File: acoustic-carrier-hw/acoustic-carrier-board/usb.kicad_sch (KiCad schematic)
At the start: 30 parts, among them J4 TYPE-C-31-M-12, U15 USB3300-EZK, U6 TS3USB30EDGSR, Y3 Crystal_GND24_Small

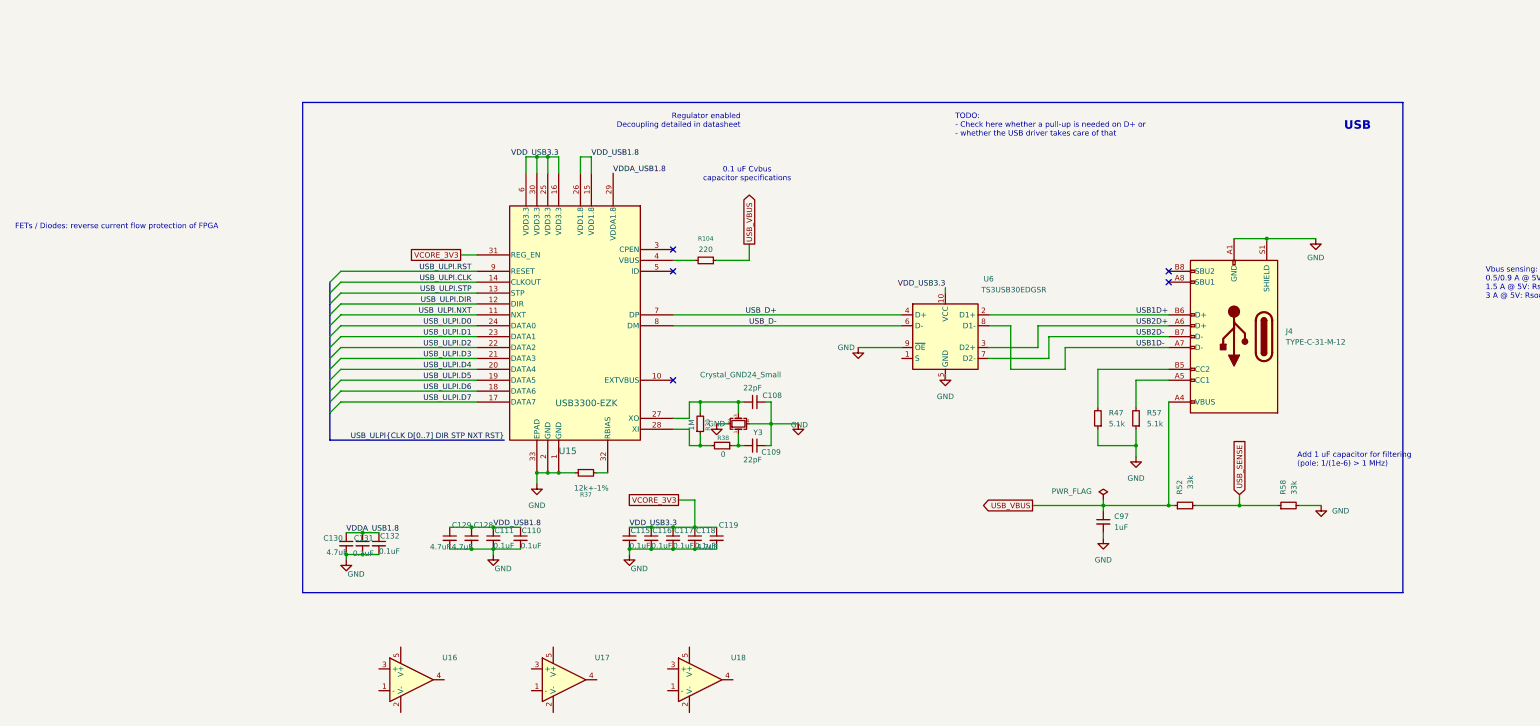
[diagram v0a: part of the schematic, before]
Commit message: [carrier] Finished schmitt trigger for cc1 and cc2 led driver + passive power signalling
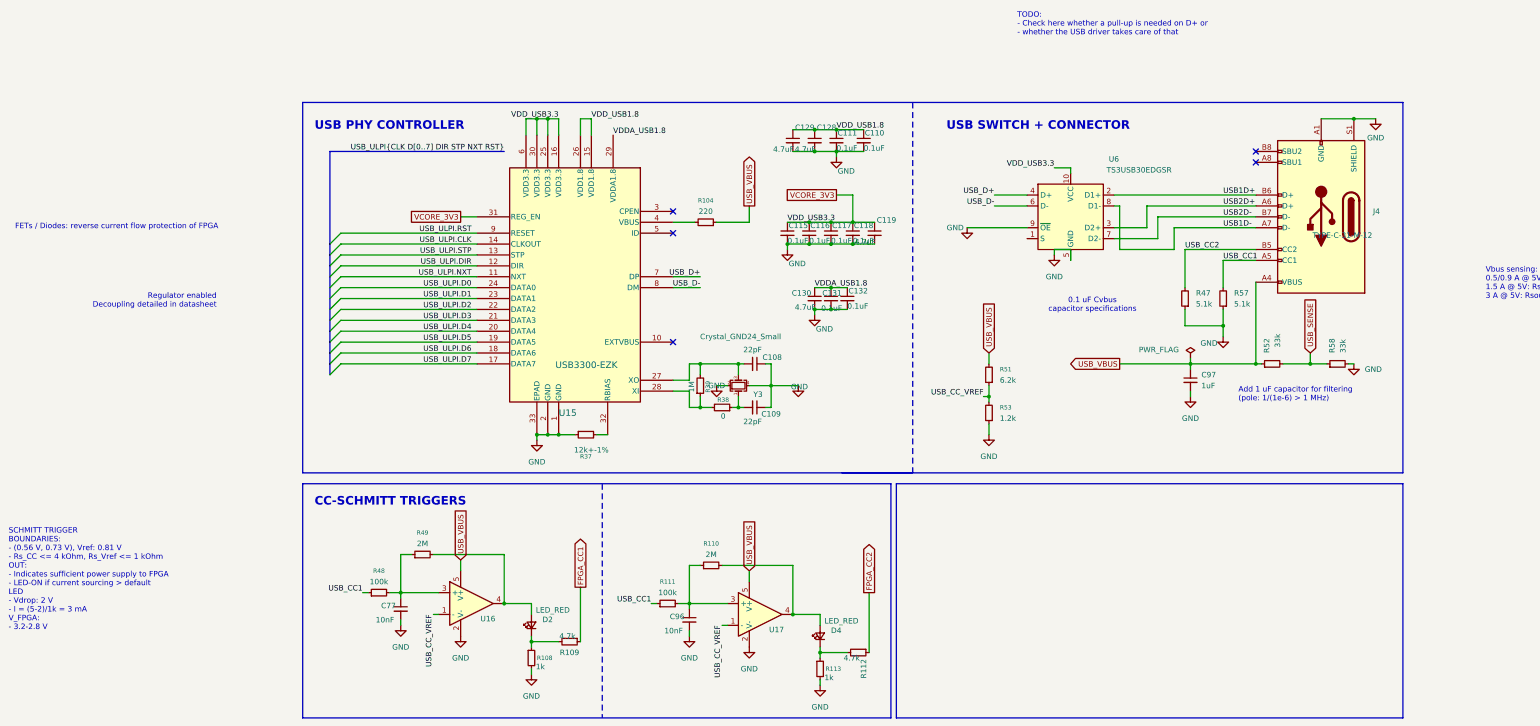
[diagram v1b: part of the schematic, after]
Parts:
- removed U18: ~, Package_TO_SOT_SMD:SOT-23-5, symbol COS3201:COS3201
- added C77, C96: 10nF, symbol Device:C_Small
- added D2, D4: LED_RED, Resistor_SMD:R_0603_1608Metric, symbol Device:LED_Small
- added R108, R113: 1k, Resistor_SMD:R_0603_1608Metric, symbol Device:R_Small
- added R109, R112: 4.7k, Resistor_SMD:R_0402_1005Metric, symbol Device:R_Small
- added R110, R49: 2M, Resistor_SMD:R_0603_1608Metric_Pad0.98x0.95mm_HandSolder, symbol Device:R_Small
- added R111, R48: 100k, Resistor_SMD:R_0603_1608Metric_Pad0.98x0.95mm_HandSolder, symbol Device:R_Small
- added R51: 6.2k, Resistor_SMD:R_0603_1608Metric_Pad0.98x0.95mm_HandSolder, symbol Device:R_Small
- added R53: 1.2k, Resistor_SMD:R_0603_1608Metric_Pad0.98x0.95mm_HandSolder, symbol Device:R_Small
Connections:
- net GND: now also U16.2 (V-), U17.2 (V-), C77.2, C96.2, R108.2, R113.2, R53.1
- net USB_VBUS: now also U16.5 (V+), U17.5 (V+), R51.2
- net USB_CC1: now reaches J4.A5 (CC1), R57.2
- net USB_CC1: now also R111.1, R48.1
- net USB_CC2: now reaches J4.B5 (CC2), R47.2
- net USB_CC_VREF: now reaches U17.1 (-)
- net USB_CC_VREF: now also U16.1 (-), R51.1, R53.2
- net at U17.3 (+): now also C96.1, R110.1, R111.2
- net at U17.4: now also D4.2 (A), R110.2
- net at U16.3 (+): now also C77.1, R48.2, R49.1
- net at U16.4: now also D2.2 (A), R49.2
- new net: D2.1 (K), R108.1, R109.2
- new net: D4.1 (K), R112.2, R113.1
- new net FPGA_CC1: R109.1
- new net FPGA_CC2: R112.1
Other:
- note added: "SCHMITT TRIGGER BOUNDARIES: - (0.56 V, 0.73 V), Vref: 0.81 V - Rs_CC <= 4 kOhm, Rs_Vref <= 1 kOhm OUT: - Indicates sufficient power supply to FPGA - LED-ON if current sourcing > default LED - Vdrop: 2 V - I = (5-2)/1k = 3 mA V_FPGA: - 3.2-2.8 V"
- moved on the sheet: C108, C109, C110, C111, C115, C116, C117, C118, C119, C128, C129, C130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

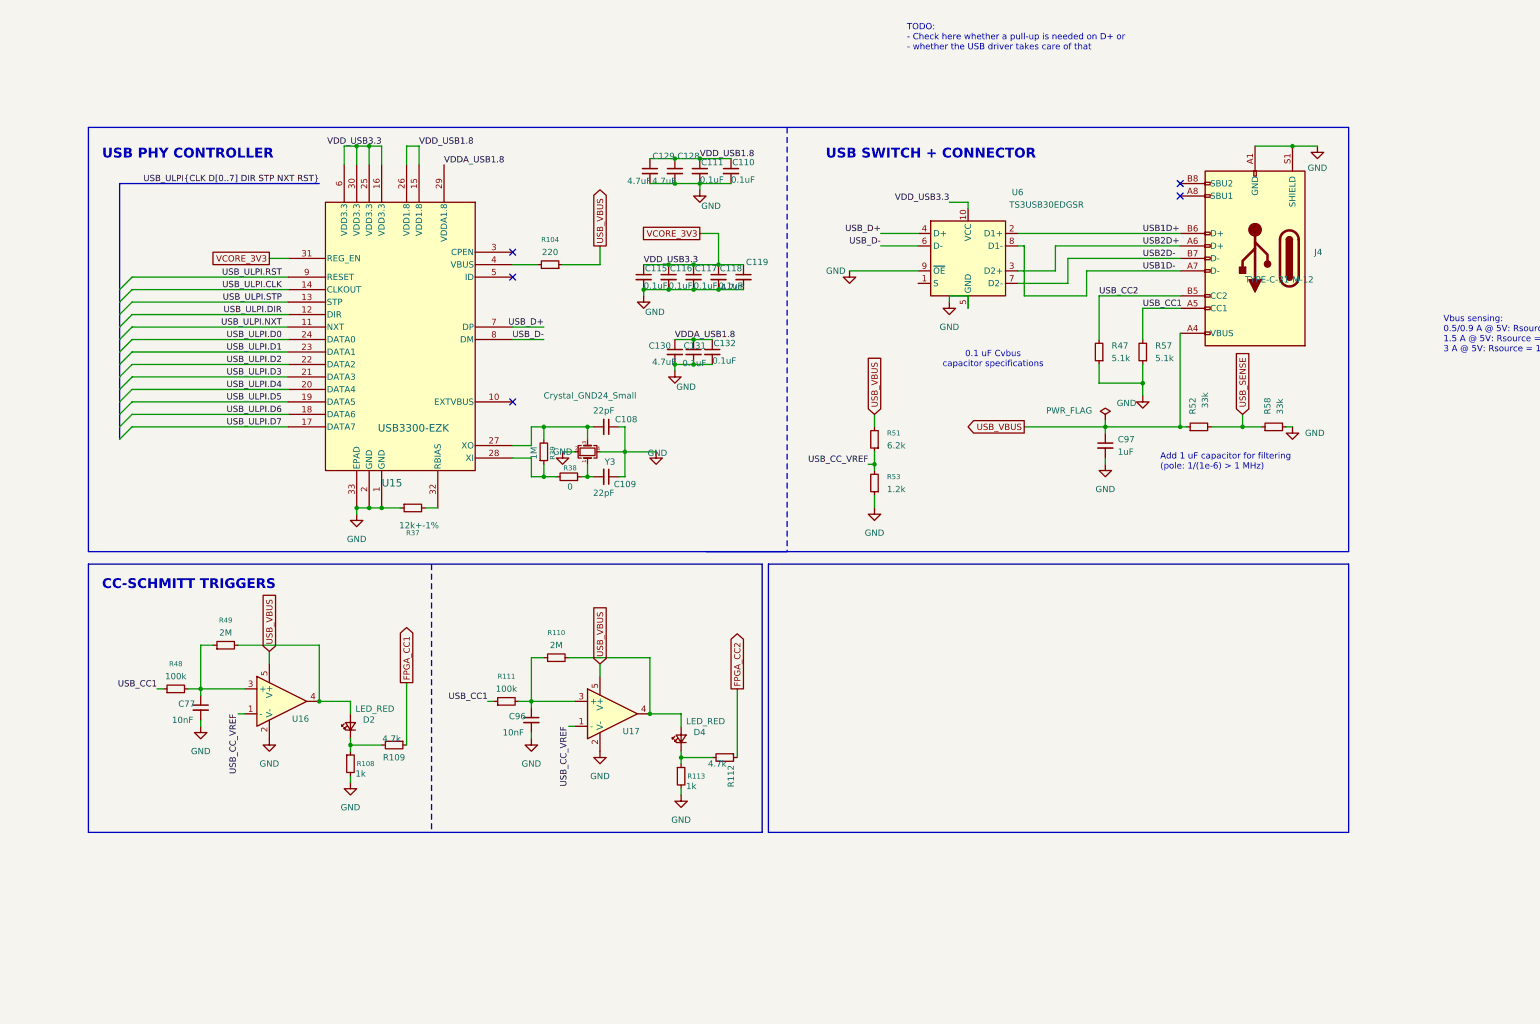
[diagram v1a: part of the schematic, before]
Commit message: [carrier] Added schmitt trigger for switch (next) check if well-connected (polarity)
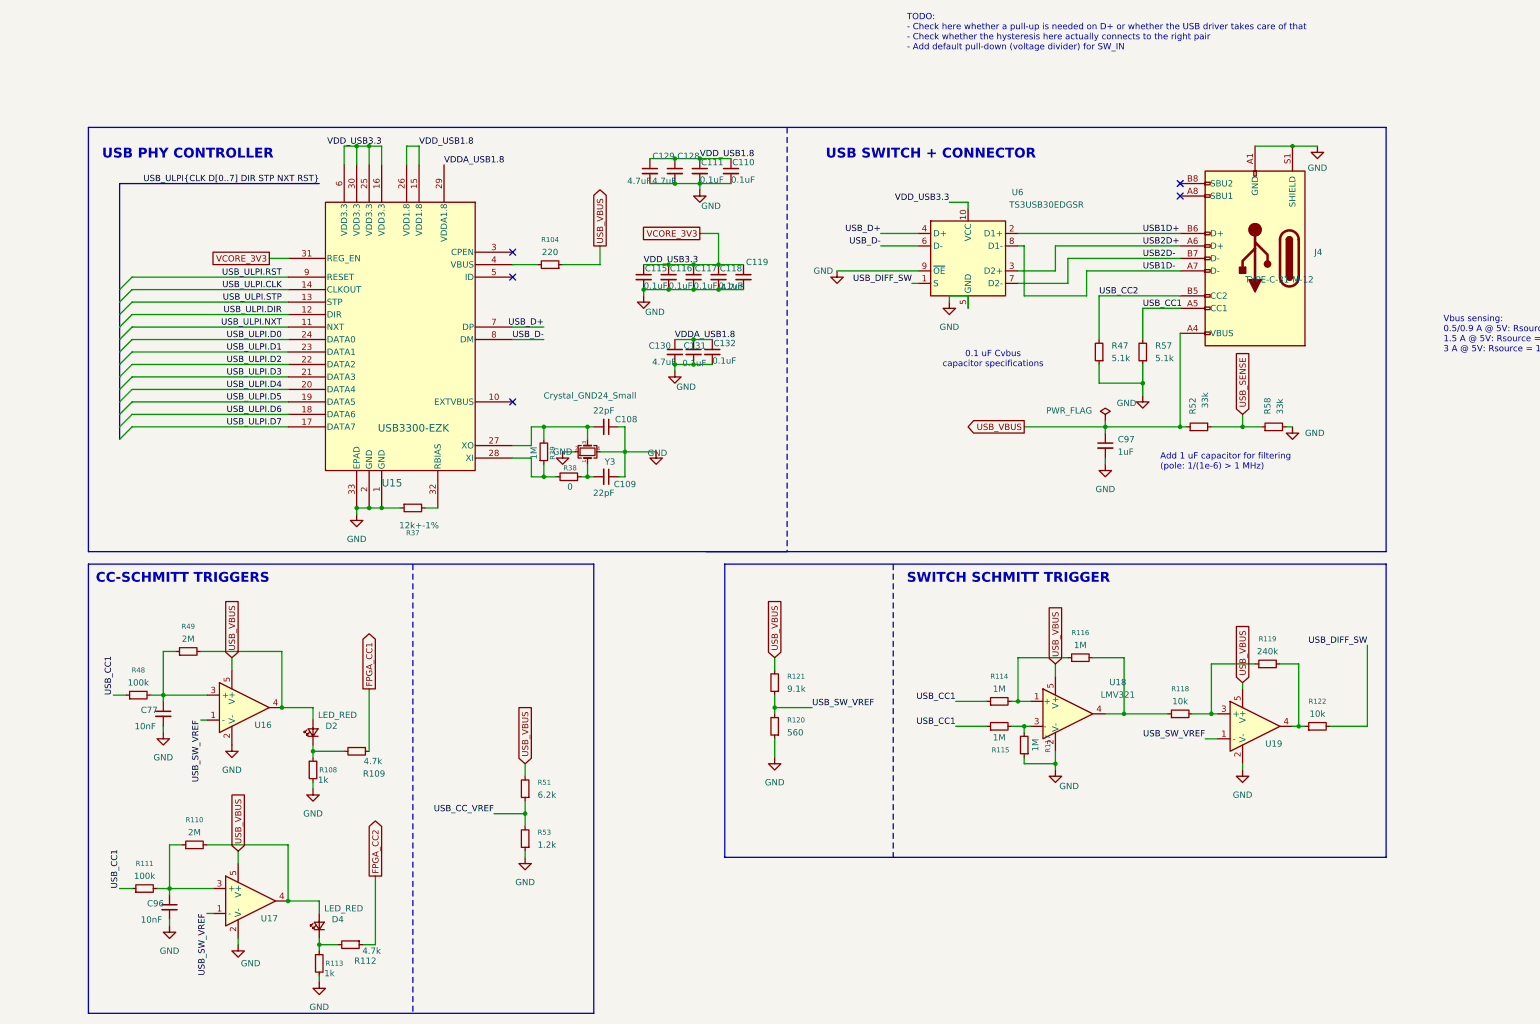
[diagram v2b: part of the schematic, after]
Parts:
- added R114, R115, R116, R117: 1M, Resistor_SMD:R_0603_1608Metric_Pad0.98x0.95mm_HandSolder, symbol Device:R_Small
- added R118, R122: 10k, Resistor_SMD:R_0603_1608Metric, symbol Device:R_Small
- added R119: 240k, Resistor_SMD:R_0603_1608Metric, symbol Device:R_Small
- added R120: 560, Resistor_SMD:R_0603_1608Metric_Pad0.98x0.95mm_HandSolder, symbol Device:R_Small
- added R121: 9.1k, Resistor_SMD:R_0603_1608Metric_Pad0.98x0.95mm_HandSolder, symbol Device:R_Small
- added U18: LMV321, Package_TO_SOT_SMD:SOT-23-5, symbol Amplifier_Operational:LMV321
- added U19: ~, Package_TO_SOT_SMD:SOT-23-5, symbol COS3201:COS3201
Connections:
- net GND: now also R117.1, R120.1, U18.2 (V-), U19.2 (V-)
- net USB_CC1: now also R114.1, R115.1
- net USB_CC_VREF: no longer U16.1 (-), U17.1 (-)
- net USB_VBUS: now also R121.2, U18.5 (V+), U19.5 (V+)
- net USB_DIFF_SW: now reaches U6.1 (S)
- net USB_DIFF_SW: now also R122.2
- new net: R114.2, R116.1, U18.1 (+)
- new net: R115.2, R117.2, U18.3 (-)
- new net: R116.2, R118.1, U18.4
- new net: R119.2, R122.1, U19.4
- new net: R118.2, R119.1, U19.3 (+)
- new net USB_SW_VREF: R120.2, R121.1, U16.1 (-), U17.1 (-), U19.1 (-)
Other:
- note added: "TODO: - Check here whether a pull-up is needed on D+ or whether the USB driver takes care of that - Check whether the hysteresis here actually connects to the right pair - Add default pull-down (voltage divider) for SW_IN"
- note removed: "TODO: - Check here whether a pull-up is needed on D+ or - whether the USB driver takes care of that"
- moved on the sheet: C77, C96, D2, D4, R108, R109, R110, R111, R112, R113, R48, R49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

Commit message: [carrier] Reorganized schematic, moPut adc signals in bus, fixed DRC errors (next) recheck ethernet, check usb, add power switch
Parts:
- removed C108, C109: 22pF, Capacitor_SMD:C_0402_1005Metric, symbol Device:C_Small
- removed C110, C111, C115: 0.1uF, Capacitor_SMD:C_0402_1005Metric, symbol Device:C_Small
- removed J4: TYPE-C-31-M-12, Connector_USB:USB_C_Receptacle_HRO_TYPE-C-31-M-12, symbol Connector:USB_C_Receptacle_USB2.0_16P
- added C137, C138, C139, C147, C148: 0.1uF, Capacitor_SMD:C_0402_1005Metric, symbol Device:C_Small
- added C140, C141: 4.7uF, Capacitor_SMD:C_0402_1005Metric, symbol Device:C_Small
- added IC1: ECP5-BGA256, fpga:BGA256C80P16X16_1400X1400X170, symbol ecp5bga256:ECP5-BGA256
- added J6: USB-C connector, Connector_USB:USB_C_Receptacle_HRO_TYPE-C-31-M-12, symbol USB_C:USB_C_Receptacle_USB2.0_16P
- added R123: 51, Resistor_SMD:R_0603_1608Metric, symbol Device:R_Small
- added R124: 10k, Resistor_SMD:R_0603_1608Metric, symbol Device:R_Small
- C116: value 0.1uF -> 10nF; LPN C307331 -> CL05B103KB5NNNC; MPN CL05B104KB54PNC -> C15195
- C117, C118: value 0.1uF -> 22pF; LPN C307331 -> C1555; MPN CL05B104KB54PNC -> 0402CG220J500NT
- C119, C128, C129, C130: value 4.7uF -> 0.1uF; LPN C23733 -> C307331; MPN CL05A475MP5NRNC -> CL05B104KB54PNC
- C131, C132: value 0.1uF -> 4.7uF; LPN C307331 -> C23733; MPN CL05B104KB54PNC -> CL05A475MP5NRNC
- C77, C96: footprint (none) -> Capacitor_SMD:C_0402_1005Metric; LPN (none) -> CL05B103KB5NNNC; MPN (none) -> C15195
- C97: value 1uF -> 0.1uF; footprint Capacitor_SMD:C_0805_2012Metric -> Capacitor_SMD:C_0402_1005Metric; LPN C28323 -> C307331; MPN CL21B105KBFNNNE -> CL05B104KB54PNC; Manufacturing part number CL31B105KBHNNNE -> (none)
- D2, D4: footprint Resistor_SMD:R_0603_1608Metric -> LED_SMD:LED_0603_1608Metric
- R104: value 220 -> 12k+-1%; LPN C22962 -> C22790; MPN 0603WAF2200T5E -> 0603WAF1202T5E
- R122: value 10k -> 1k; LPN C25804 -> C21190; MPN 0603WAF1002T5E -> 0603WAF1001T5E
- R37: value 12k+-1% -> 220; LPN C22790 -> C22962; MPN 0603WAF1202T5E -> 0603WAF2200T5E
- R38: value 0 -> 1M; footprint Resistor_SMD:R_0402_1005Metric_Pad0.72x0.64mm_HandSolder -> Resistor_SMD:R_0402_1005Metric; LPN C17168 -> C26083; MPN 0402WGF0000TCE -> 0402WGF1004TCE
- R39: value 1M -> 0; footprint Resistor_SMD:R_0402_1005Metric -> Resistor_SMD:R_0402_1005Metric_Pad0.72x0.64mm_HandSolder; LPN C26083 -> C17168; MPN 0402WGF1004TCE -> 0402WGF0000TCE
- U15: Iconsumption (none) -> 54.7mA
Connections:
- net FPGA_CC1: now also IC1.R13 (PR41C)
- net FPGA_CC2: now also IC1.T14 (PR41D)
- net GND: now also C117.1, C118.1, R104.1, C137.2, C138.2, C139.2, C140.2, C141.2, C147.2, C148.2, J6.A1 (GND), J6.A12 (GND), J6.B1 (GND), J6.B12 (GND), J6.S1 (SHIELD), R123.1, R124.1; no longer C117.2, C118.2, R37.1, U6.9 (~{OE})
- net USB_CC1: now also J6.A5 (CC1); no longer R115.1
- net USB_CC2: now also R115.1, J6.B5 (CC2)
- net USB_DIFF_SW: now also R124.2
- net USB_SENSE: now also IC1.R12 (PR44A/RDQS44)
- net USB_ULPI.CLK: now also IC1.P15 (PR32B/RDQSN32)
- net USB_ULPI.D0: now also IC1.R16 (PR35B/VREF1_3)
- net USB_ULPI.D1: now also IC1.M13 (PR35C)
- net USB_ULPI.D2: now also IC1.N14 (PR35D/RDQ32)
- net USB_ULPI.D3: now also IC1.N13 (PR38A/RDQ44)
- net USB_ULPI.D4: now also IC1.P14 (PR38B)
- net USB_ULPI.D5: now also IC1.R15 (PR38C)
- net USB_ULPI.D6: now also IC1.T15 (PR38D)
- net USB_ULPI.D7: now also IC1.P13 (PR41A)
- net USB_ULPI.DIR: now also IC1.M14 (PR32D)
- net USB_ULPI.NXT: now also IC1.P16 (PR35A)
- net USB_ULPI.RST: now also IC1.N16 (PR32A/RDQS32)
- net USB_ULPI.STP: now also IC1.L14 (PR32C)
- net USB_VBUS: now also R37.1, J6.A4 (VBUS), J6.A9 (VBUS), J6.B4 (VBUS), J6.B9 (VBUS); no longer R104.1
- net VCORE_3V3: now also C128.1, C129.1, C130.1, C131.1, C137.1, IC1.K11 (VCCIO3_1), IC1.L11 (VCCIO3_2); no longer C117.1, C118.1
- net VDDA_USB1.8: now also C138.1, C139.1; no longer C130.1, C131.1
- net VDD_USB1.8: now also C140.1, C141.1, C147.1, C148.1; no longer C128.1, C129.1
- net at U15.27 (XO), Y3.3: now also C117.2, R38.2; no longer R39.2
- net at U15.32 (RBIAS): now also R104.2; no longer R37.2
- net at Y3.1: now also C118.2, R39.1; no longer R38.1
- net at U15.4 (VBUS): now also R37.2; no longer R104.2
- net USB1D+ renamed USBDP2
- net USBDP2: now also J6.B6 (DP2)
- net USB1D- renamed USBDN2
- net USBDN2: now also J6.B7 (DN2)
- net USB2D+ renamed USBDP1
- net USBDP1: now also J6.A6 (DP1)
- net USB2D- renamed USBDN1
- net USBDN1: now also J6.A7 (DN1)
- net USB_D+ renamed USB_DP
- net USB_D- renamed USB_DM
- new net: R123.2, U6.9 (~{OE})
- new net: R38.1, R39.2, U15.28 (XI)
- no-connect marks 5 -> 21
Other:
- note added: "SELECT: - LOW: D1 - HIGH: D2"
- note added: "SWITCH - 51 ohm @ unused pins (avoid reflections) Switching voltage - 1.7-Vcc - Max Voltage: 7 V"
- note added: "USB_CC1: high -> USB_DIFF_SW: high -> D2 ACTIVE USB_CC2: high -> USB_DIFF_SW: low -> D1 ACTIVE"
- note removed: "Add 1 uF capacitor for filtering (pole: 1/(1e-6) > 1 MHz)"
- note removed: "FETs / Diodes: reverse current flow protection of FPGA"
- moved on the sheet: D2, D4, R108, R109, R110, R111, R112, R113, R114, R115, R116, R117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
